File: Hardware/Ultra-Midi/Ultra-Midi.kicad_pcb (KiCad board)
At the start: 2 copper layers, 57.5 x 20 mm, 28 parts, among them J1 Conn_01x02, J14 CUI_SD-50BV, J16 CUI_SD-50BV, J17 CUI_SD-50BV, J2 Conn_01x02, J3 Conn_01x02, J4 Conn_01x06, U1 ADuM226, U2 AP7370

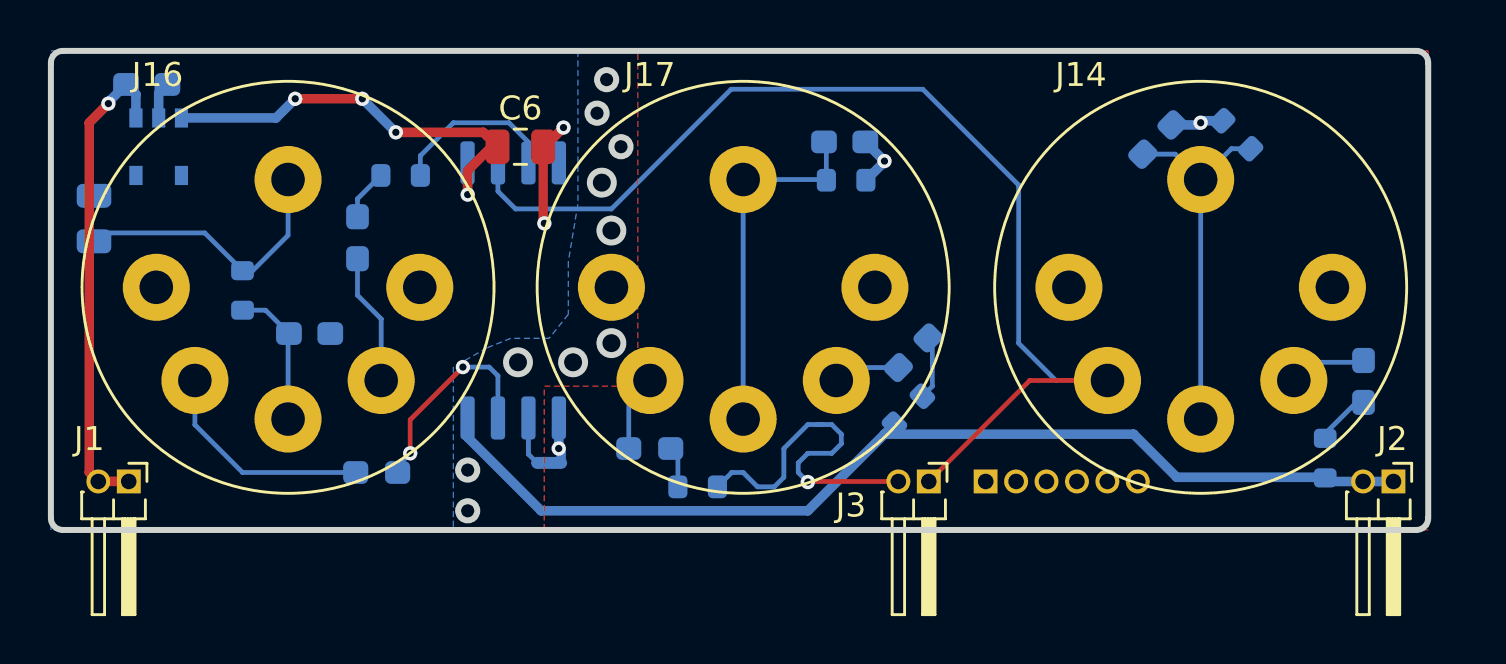
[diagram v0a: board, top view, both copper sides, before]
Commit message: Redesigned VDP-board to include a socket, increased it to 4 layers. Various clean-ups here and there. Improved the printer-port and joystick-port 3D-models. Improved the cooling-fin 3D-model, and added attachment-spring in 3D-model.
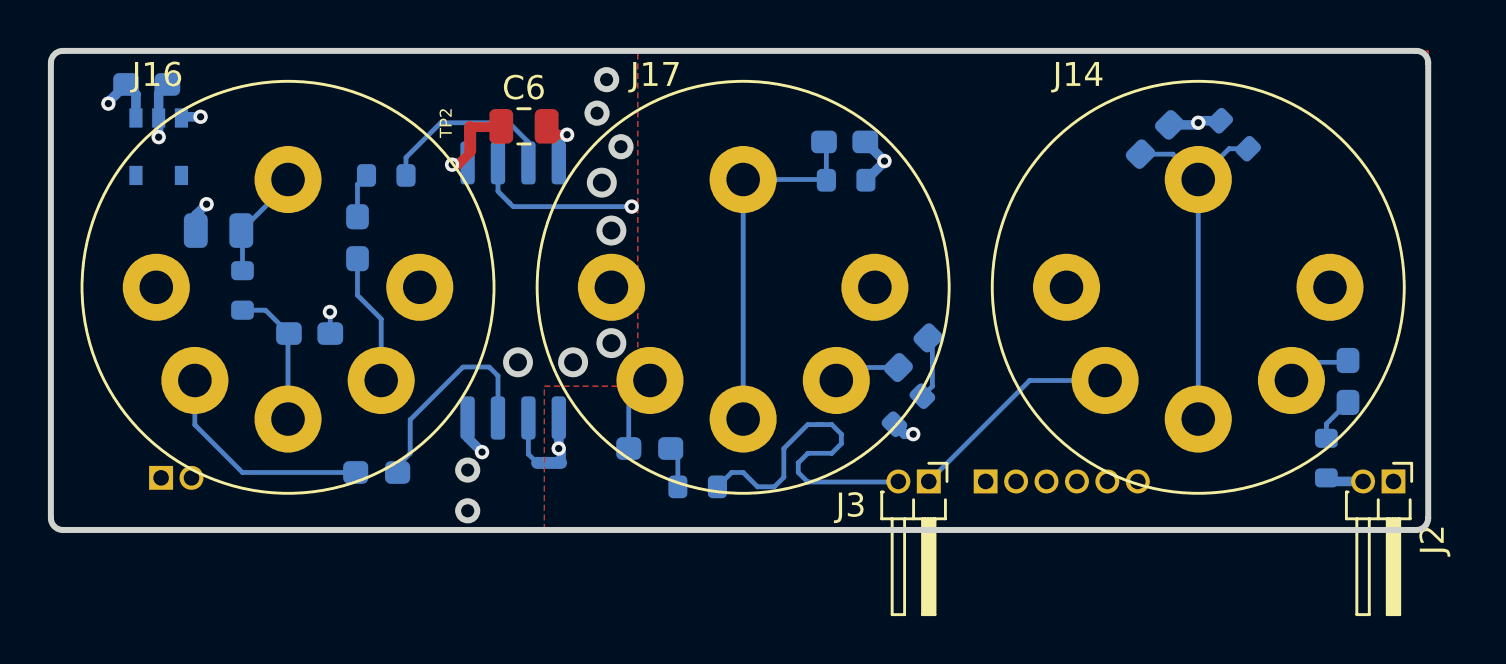
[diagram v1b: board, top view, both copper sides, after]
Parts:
- added TP2: TestPoint_2Pole, NetTie:NetTie-2_SMD_Pad0.5mm, F.Cu at (133.5, 81.7)
- J1: moved to B.Cu
- moved C4 5.22 mm to (123.0, 85.5), turned to 180 degrees
- moved J1 1.36 mm to (120.6, 95.8)
- moved C6 0.86 mm to (135.8, 81.2)
- moved FB4 0.65 mm to (170.2, 91.8)
- moved R3 0.60 mm to (130.0, 83.2)
- moved C1 0.10 mm to (162.1, 81.7)
- moved J14 0.10 mm to (163.9, 87.9)
- moved R2 0.10 mm to (165.4, 81.5)
- moved R1 0.05 mm to (169.2, 95.0)
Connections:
- U1 pad 1: +5VD -> /+5VD_
- U2 pad 3: +5VD -> /+5VD_
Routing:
- net +5VD: track 18.2 -> 1.32 mm, vias 4 -> 0
- net /+5VD_: track 0.00 -> 13.9 mm, vias 0 -> 2
- net /MID_RX: track 47.1 -> 36.2 mm, vias 0 -> 1
- net Net-(C4-Pad1): track 11.8 -> 4.63 mm
- net +5V: track 43.5 -> 45.4 mm, vias 0 -> 2
- net +12V: track 20.2 -> 21.4 mm
- net Earth: track 5.95 -> 6.73 mm, vias 2 -> 4
- net Net-(FB4-Pad1): track 3.26 -> 2.60 mm
- net /CSRCi: track 7.10 -> 7.66 mm
- net /MID_TX: vias 1 -> 0
- net /CSINKi: vias 2 -> 0
- added copper zone on In1.Cu, net Earth
- removed copper zone on B.Cu, net Earth
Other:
- copper layers 2 -> 4
- rule pad_to_mask_clearance: 0 -> 0.05
